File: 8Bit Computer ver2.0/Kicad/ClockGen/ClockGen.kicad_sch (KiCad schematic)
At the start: 9 parts, among them IC1 SN74LVC1GU04DCKR, IC2 SN74LVC1G14DBVR, Y1 8MHz

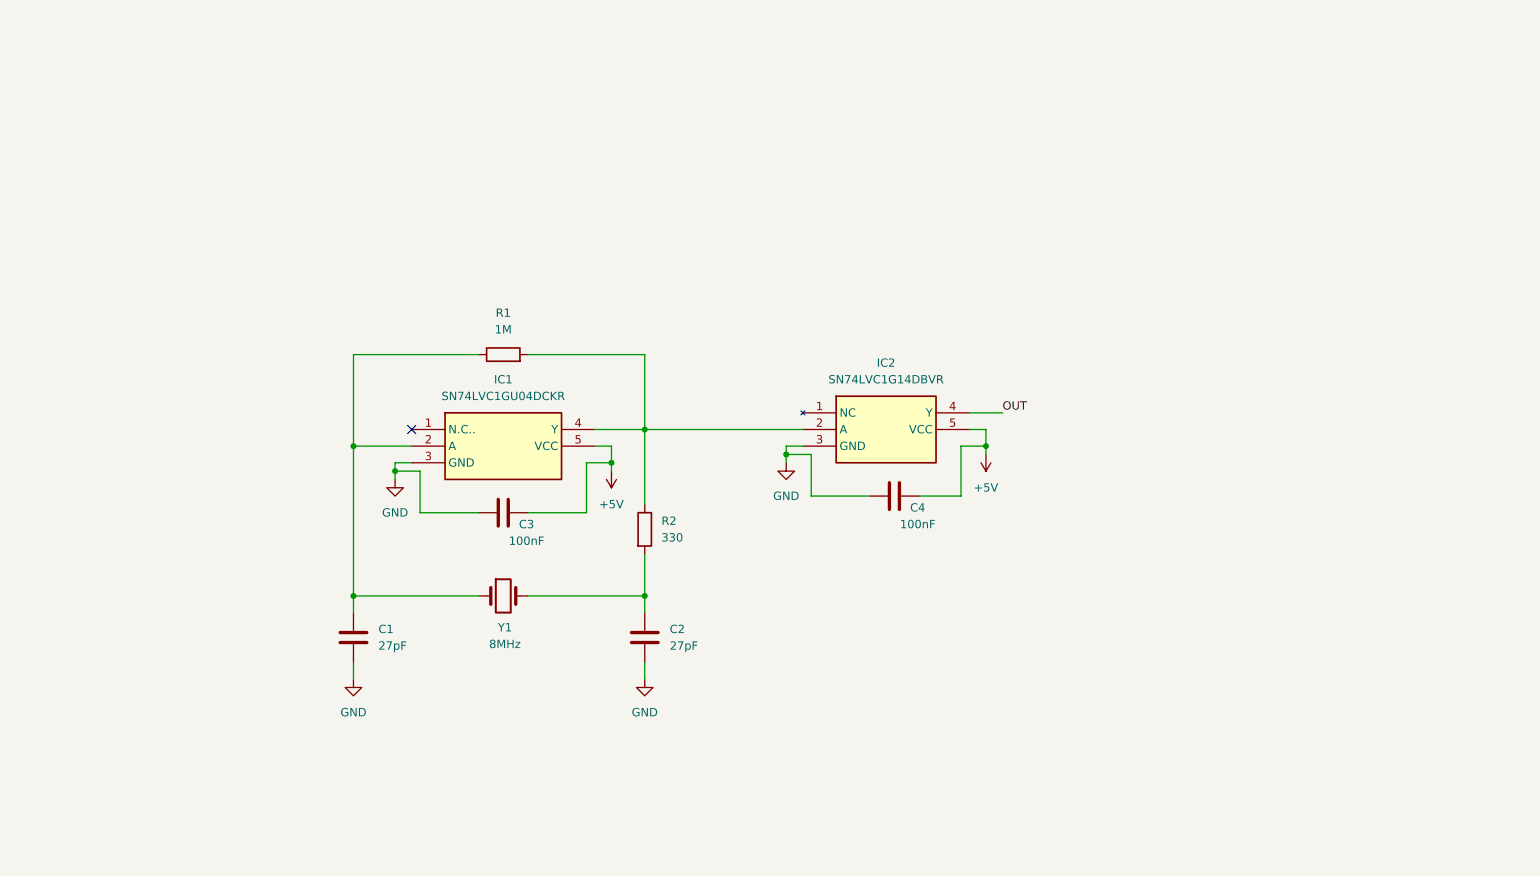
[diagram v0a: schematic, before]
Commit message: Kicad, parts
parts:
added Mux 4:1 for CLK
added LM555
Kicad:
added some Diodes for Flash disable
fixed wrong routing of flag register
fixed wrong routing of STC STF in INC/AddS
LM555 circuit for 1Hz to 100Hz
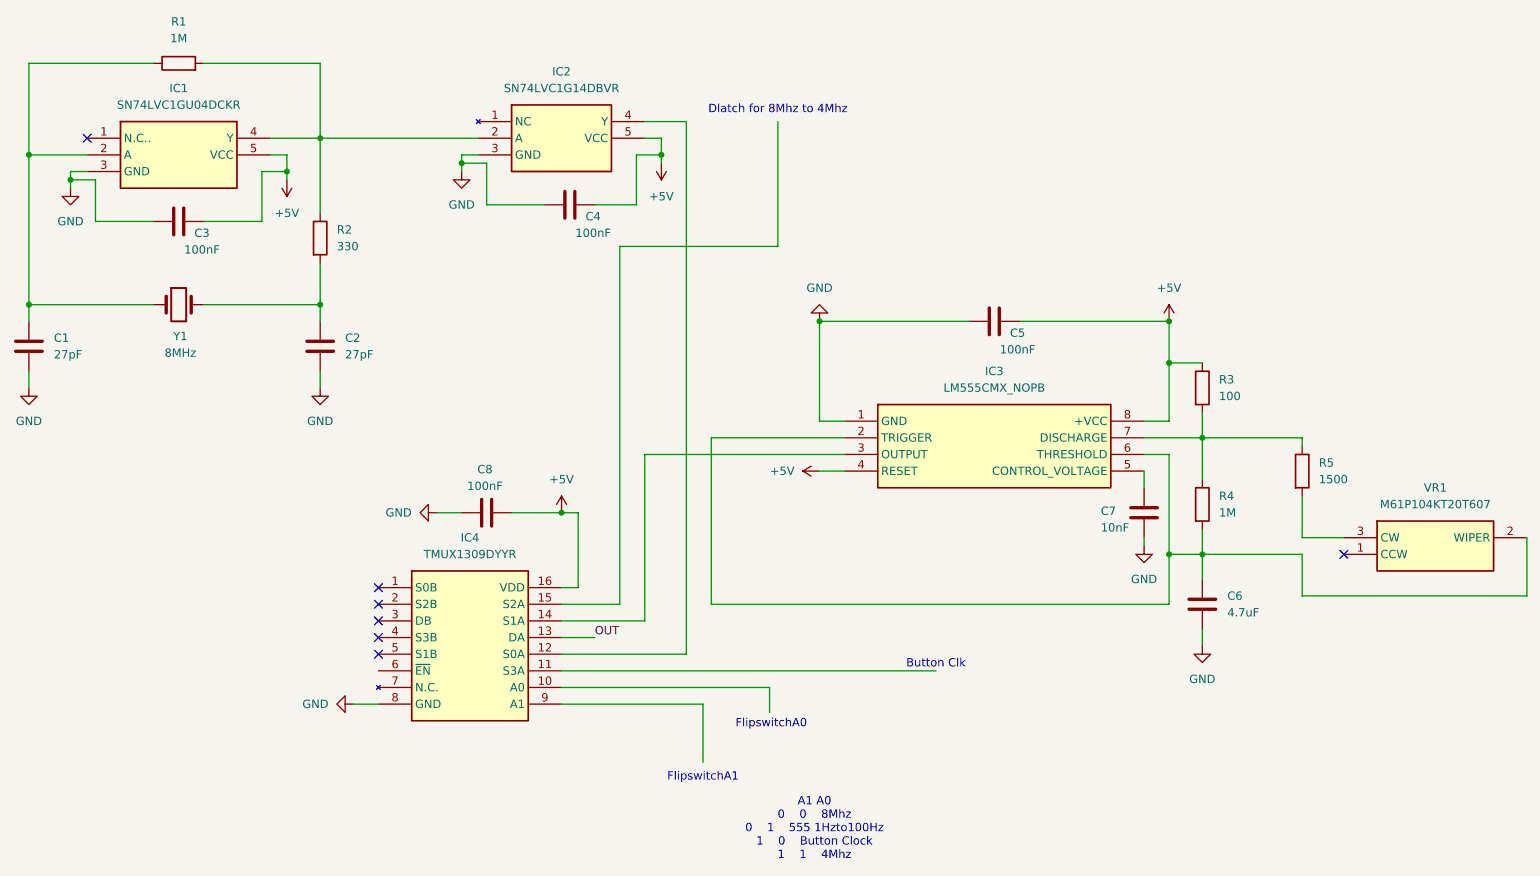
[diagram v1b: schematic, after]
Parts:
- added C5, C8: 100nF, Capacitor_SMD:C_1206_3216Metric_Pad1.33x1.80mm_HandSolder, symbol Device:C
- added C6: 4.7uF, Capacitor_SMD:C_1206_3216Metric_Pad1.33x1.80mm_HandSolder, symbol Device:C
- added C7: 10nF, Capacitor_SMD:C_1206_3216Metric_Pad1.33x1.80mm_HandSolder, symbol Device:C
- added IC3: LM555CMX_NOPB, Samacsys:SOIC127P600X175-8N, symbol Samacsys:LM555CMX_NOPB
- added IC4: TMUX1309DYYR, Samacsys:SOP50P326X110-16N, symbol Samacsys:TMUX1309DYYR
- added R3: 100, Resistor_SMD:R_1206_3216Metric_Pad1.30x1.75mm_HandSolder, symbol Device:R
- added R4: 1M, Resistor_SMD:R_1206_3216Metric_Pad1.30x1.75mm_HandSolder, symbol Device:R
- added R5: 1500, Resistor_SMD:R_1206_3216Metric_Pad1.30x1.75mm_HandSolder, symbol Device:R
- added VR1: M61P104KT20T607, Samacsys:M61P104KT20T607, symbol Samacsys:M61P104KT20T607
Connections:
- net +5V: now also C5.1, C8.1, IC3.4 (RESET), IC3.8 (+VCC), IC4.16 (VDD), R3.1
- net GND: now also C5.2, C6.2, C7.2, C8.2, IC3.1 (GND), IC4.8 (GND)
- net OUT: now also IC4.13 (DA); no longer IC2.4 (Y)
- new net: IC3.7 (DISCHARGE), R3.2, R4.1, R5.1
- new net: R5.2, VR1.3 (CW)
- new net: IC2.4 (Y), IC4.12 (S0A)
- new net: C6.1, IC3.2 (TRIGGER), IC3.6 (THRESHOLD), R4.2, VR1.2 (WIPER)
- new net: C7.1, IC3.5 (CONTROL_VOLTAGE)
- new net: IC3.3 (OUTPUT), IC4.14 (S1A)
- no-connect marks 1 -> 7
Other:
- note added: "A1 A0 0 0 8Mhz 0 1 555 1Hzto100Hz 1 0 Button Clock 1 1 4Mhz"
- note added: "Button Clk"
- note added: "Dlatch for 8Mhz to 4Mhz"
- note added: "FlipswitchA0"
- note added: "FlipswitchA1"
- moved on the sheet: C1, C2, C3, C4, IC1, IC2, R1, R2, Y1
